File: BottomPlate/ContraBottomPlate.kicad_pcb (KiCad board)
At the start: 2 copper layers, 231 x 76.2 mm, 10 parts, among them p1 gndingpad

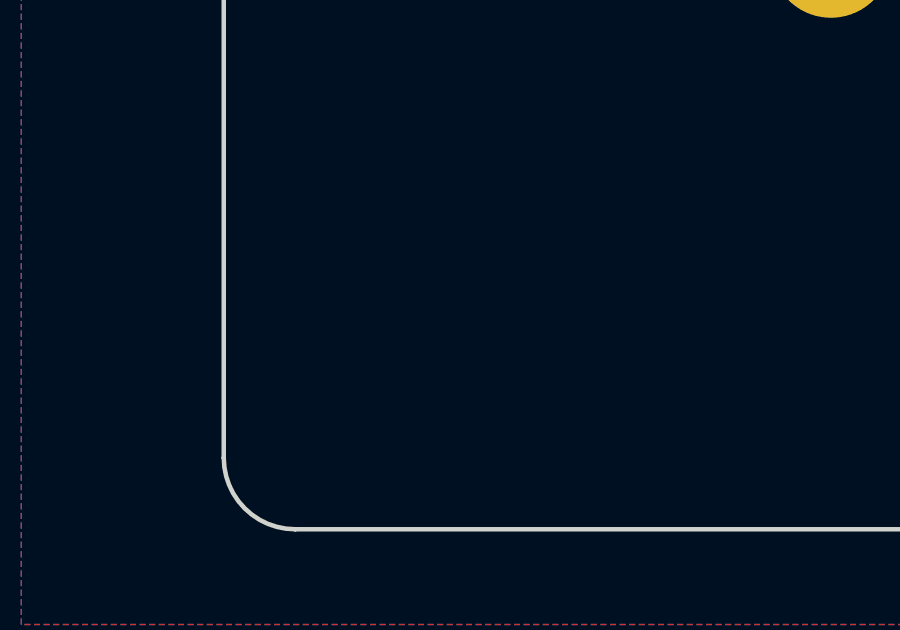
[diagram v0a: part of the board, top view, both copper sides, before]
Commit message: Update plate files to latest
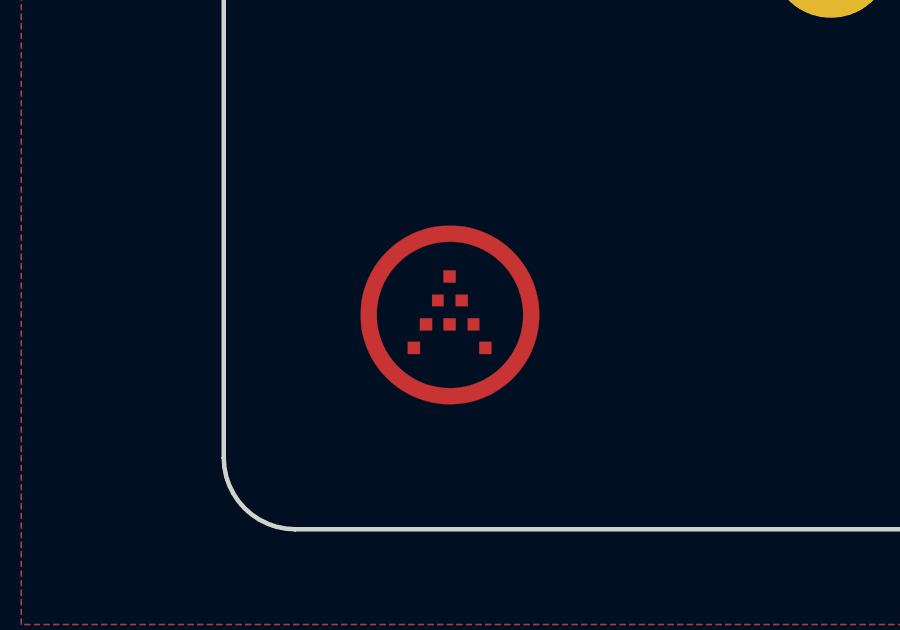
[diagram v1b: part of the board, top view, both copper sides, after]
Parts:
- removed the G*** at (115.9, 100.0)
- removed the G*** at (242.1, 97.6)
- added G***: LOGO, locallib:ai-ring-6mm-FancyAss, F.Cu at (46.0, 116.7)
- added G***: LOGO, locallib:ai-ring-6mm-FancyAss-Mask, F.Cu at (46.0, 116.7)
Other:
- board text added: "Contra Keyboard by ai03"
- board text removed: "www.cartel.ltd www.ai03.me"
